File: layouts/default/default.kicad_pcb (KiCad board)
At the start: 2 copper layers, 37 x 37 mm, 110 parts

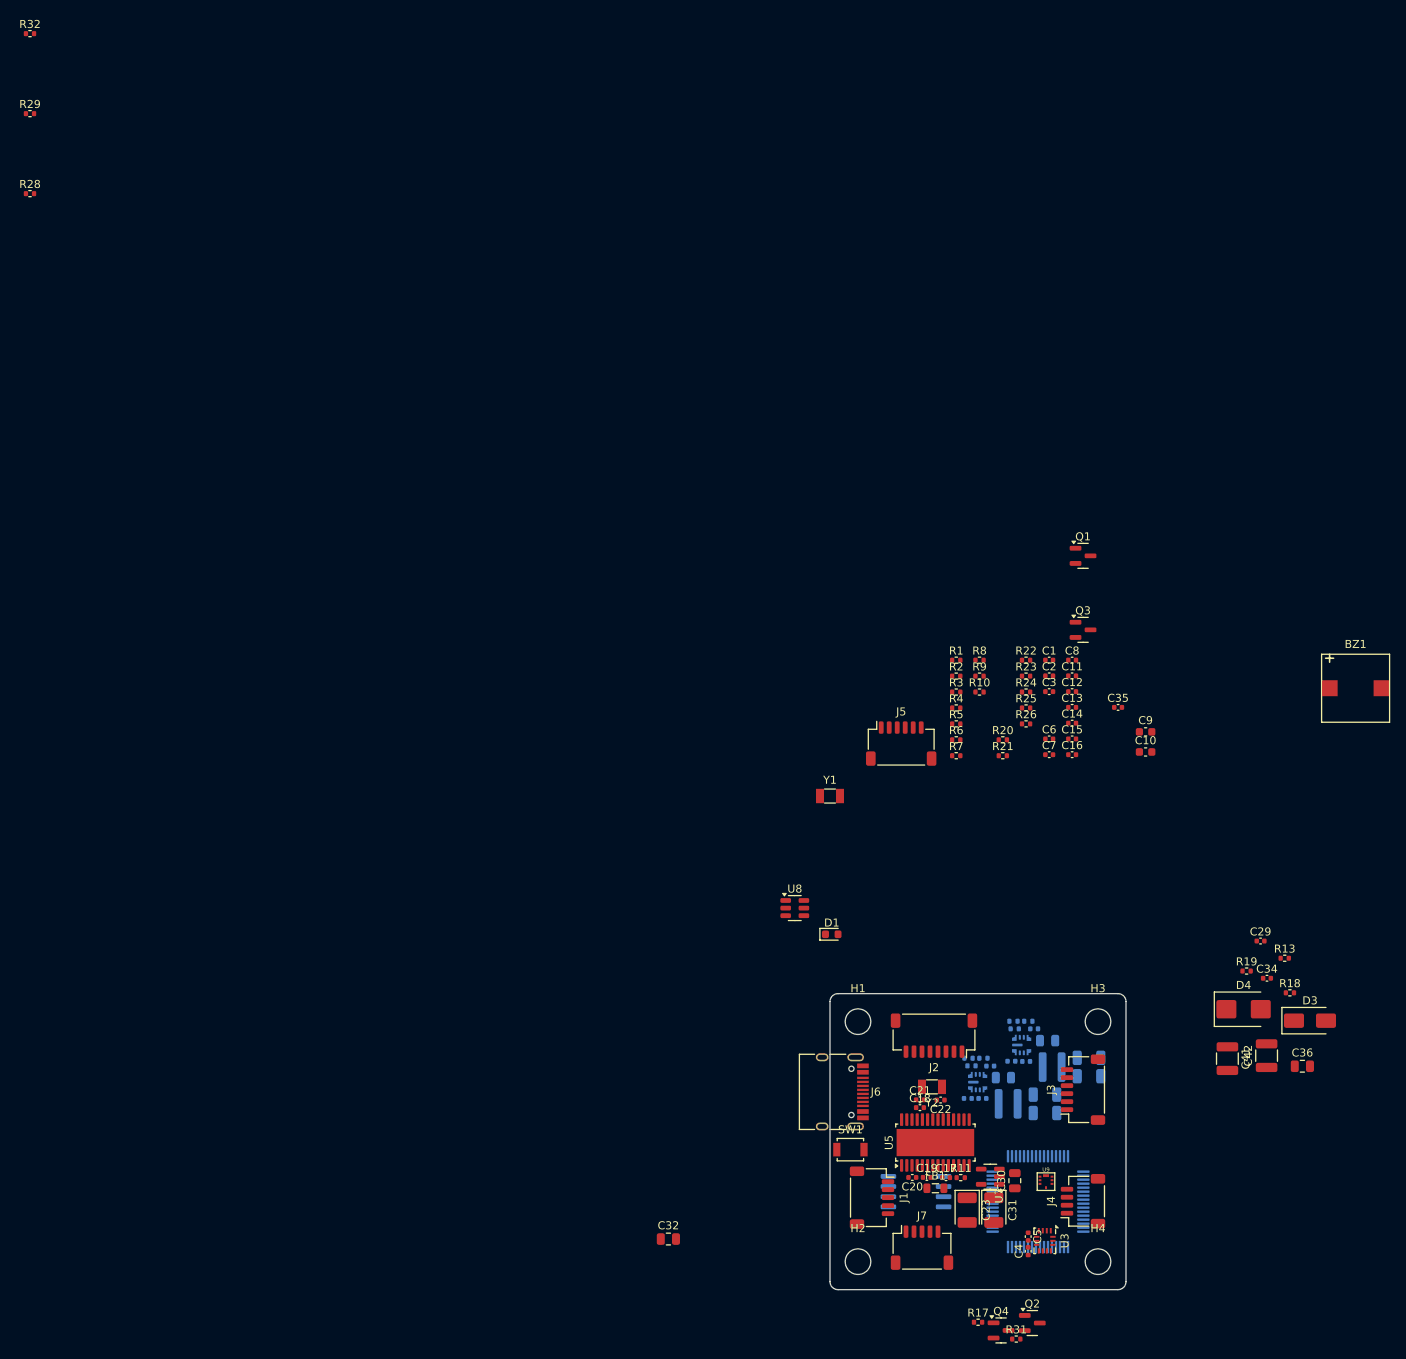
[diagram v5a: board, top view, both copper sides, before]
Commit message: Replace MLT-8530 buzzer with Same Sky CMT-4023S (NDAA, 78% smaller)
MLT-8530 (8.5x8.5mm, Chinese) replaced with CMT-4023S-SMT-TR
(4x4x2mm, Same Sky/CUI, US-headquartered, NDAA-compliant).
70dB vs 80dB SPL trade-off for 78% area reduction. Custom KiCad
footprint created. Also removed spare connector (J5) — UART3
will route to solder pads at board perimeter. Layout clusters
reorganized for remaining component placement.

Co-Authored-By: Claude Opus 4.6 <noreply@anthropic.com>
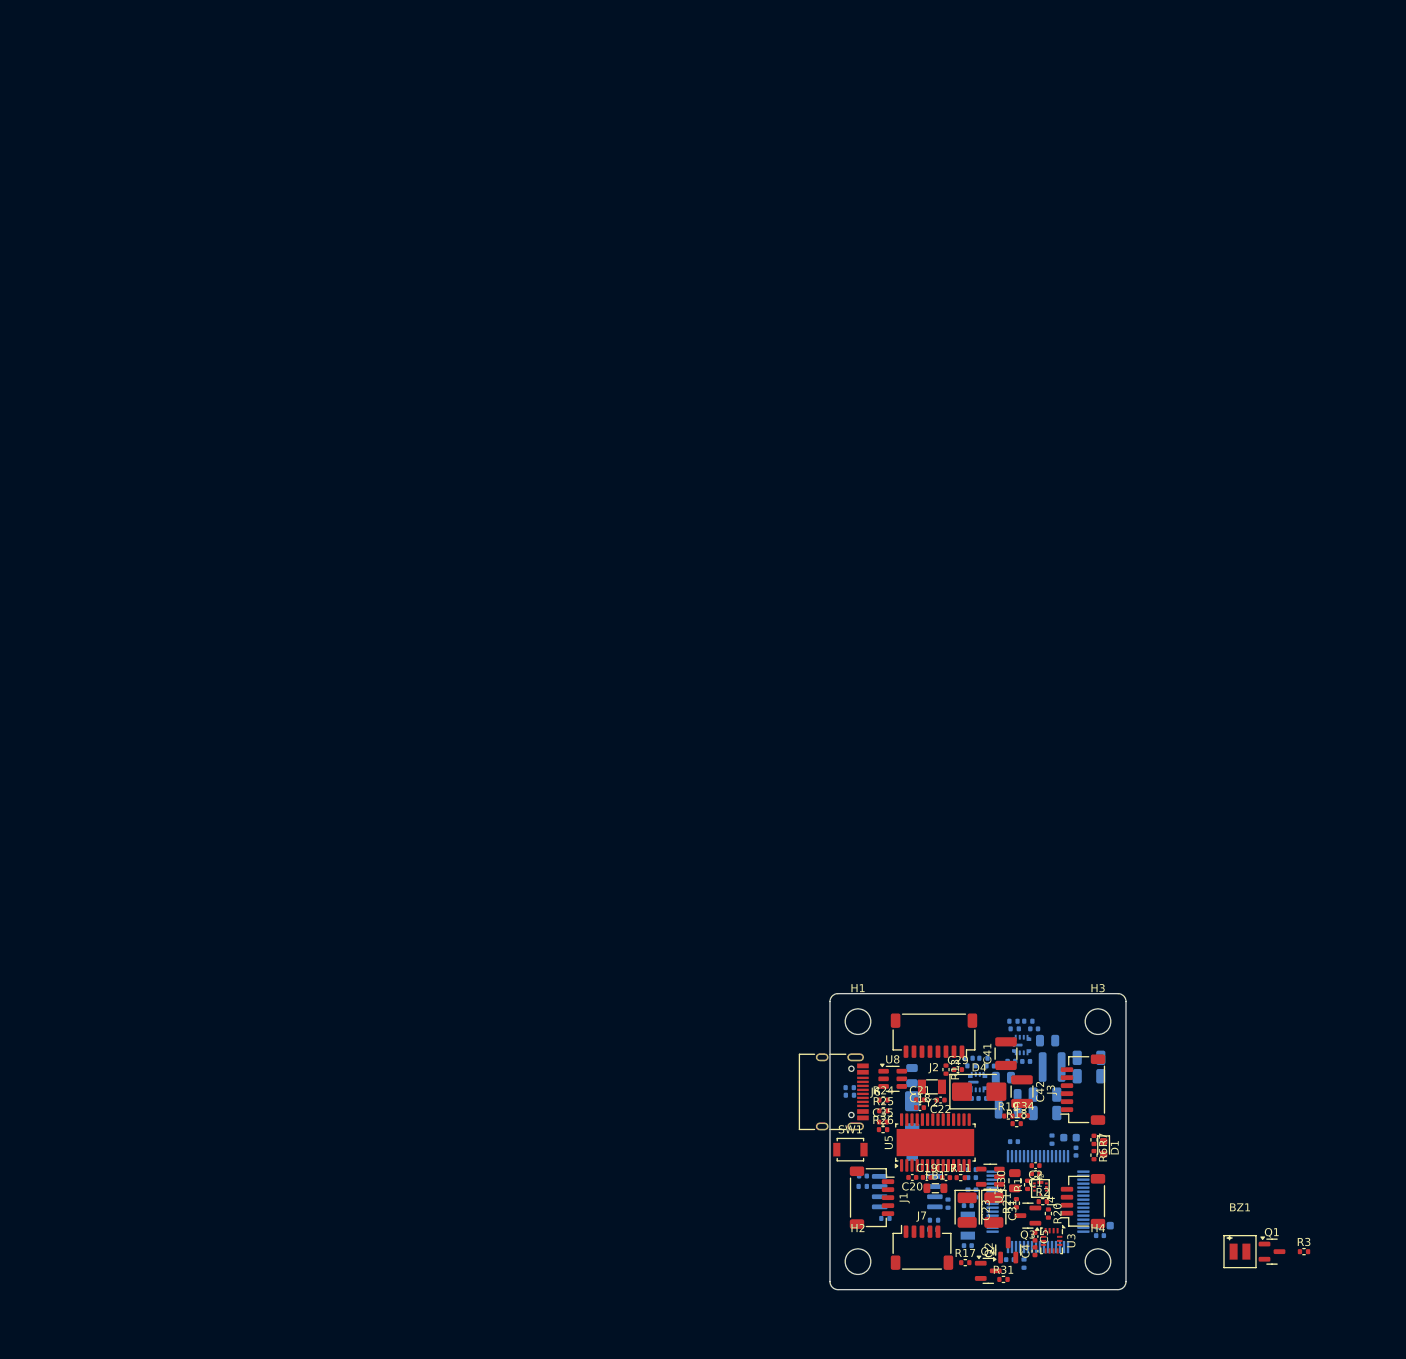
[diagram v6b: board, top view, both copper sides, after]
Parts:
- removed J5: , Connector_JST:JST_SH_SM06B-SRSS-TB_1x06-1MP_P1.00mm_Horizontal
- BZ1: footprint lib:Buzzer_SMD_MLT-8530_8.5x8.5mm -> lib:Buzzer_SMD_CMT-4023S_4x4mm
- C10, C11, C12, C13, C14, C15, C16, C3, C32, C36, C6, C7, C8, C9, D3, R10, R22, R23, R28, R29, R32, R4, R5, R8, R9, Y1: moved to B.Cu
- moved R32 182.7 mm to (106.9, 128.1)
- moved R29 178.6 mm to (113.0, 128.3)
- moved R28 171.8 mm to (112.9, 129.5), turned to 180 degrees
- moved Q1 90.1 mm to (155.2, 132.2)
- moved R3 82.4 mm to (159.2, 132.2)
- moved R8 75.6 mm to (124.2, 133.8), turned to -90 degrees
- moved Q3 73.5 mm to (124.7, 127.8), turned to 180 degrees
- moved BZ1 71.9 mm to (151.2, 132.2)
- moved C8 67.7 mm to (118.2, 125.0), turned to 90 degrees
- moved C14 67.5 mm to (122.5, 133.2)
- moved R2 66.6 mm to (126.6, 126.0)
- moved R1 66.2 mm to (124.7, 123.9), turned to 90 degrees
- moved C13 66.1 mm to (133.8, 130.2)
- moved C3 64.9 mm to (104.1, 122.8)
- moved C1 64.2 mm to (125.7, 122.5), turned to 180 degrees
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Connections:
- net v5 renamed beeper-vdd
- net vdd renamed baro-vdd
- J4 pad 3: conn-rx-2 -> conn-rx-1
- J4 pad 4: conn-tx-2 -> conn-tx-1
- R20 pad 1: conn-rx-2 -> conn-rx-1
- U4 pad 29: conn-tx-1 -> pb10
- U4 pad 30: conn-rx-1 -> pb11
- U4 pad 42: conn-tx-2 -> conn-tx-1
